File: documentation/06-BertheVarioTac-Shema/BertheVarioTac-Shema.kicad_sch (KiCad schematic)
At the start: 15 parts, among them CN1 4P-1.25 Temperature and humid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, P1 4P-1.25 Power supply base, P1 Potentiometer 10k ohms, P3 4P-1.25 Extended IO, P4 2P-1.25 SPEAK, SW1 SW_DIP_x01

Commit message: son + gps + baro ok
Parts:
- removed R1: R 100 ohms, symbol Device:R_Small
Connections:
- net GNDREF: now also CN1.4 (Pin_4)
- net at P4.1 (Pin_1): now also S1.2
- net at HMC5883L_Mag.. (VIN): now also CN1.1 (Pin_1), GPS-NEO6M. (VCC)
- net at CN1.3 (Pin_3): now also BMP180_Pres.. (VIN), HMC5883L_Mag.. (VIN)
- new net: BMP180_Pres.. (VIN), CN1.2 (Pin_2), HMC5883L_Mag.. (VIN)
- now unconnected: BMP180_Pres.. (VIN), BMP180_Pres.. (VIN), P3.2 (Pin_2)
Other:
- note removed: "NC"
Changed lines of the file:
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@@
-    (stroke (width 0) (type default))
-  )
-  (wire (pts (xy 128.27 52.07) (xy 149.86 52.07))
     (stroke (width 0) (type default))
   )
@@
     (stroke (width 0) (type default))
   )
+  (wire (pts (xy 133.35 59.69) (xy 144.78 59.69))
+    (stroke (width 0) (type default))
+  )
   (wire (pts (xy 170.18 44.45) (xy 170.18 45.72))
     (stroke (width 0) (type default))
@@
     (stroke (width 0) (type default))
   )
-  (wire (pts (xy 53.34 69.85) (xy 57.15 69.85))
-    (stroke (width 0) (type default))
-  )
-  (wire (pts (xy 149.86 73.66) (xy 161.29 73.66))
+  (wire (pts (xy 144.78 73.66) (xy 161.29 73.66))
     (stroke (width 0) (type default))
   )
@@
     (stroke (width 0) (type default))
   )
+  (wire (pts (xy 133.35 76.2) (xy 133.35 59.69))
+    (stroke (width 0) (type default))
+  )
   (wire (pts (xy 220.98 156.21) (xy 220.98 144.78))
     (stroke (width 0) (type default))
   )
-  (wire (pts (xy 149.86 52.07) (xy 149.86 73.66))
-    (stroke (width 0) (type default))
-  )
   (wire (pts (xy 196.85 27.94) (xy 196.85 29.21))
     (stroke (width 0) (type default))
   )
+  (wire (pts (xy 144.78 59.69) (xy 144.78 60.96))
+    (stroke (width 0) (type default))
+  )
   (wire (pts (xy 58.42 130.81) (xy 69.85 130.81))
     (stroke (width 0) (type default))
@@
     (stroke (width 0) (type default))
   )
+  (wire (pts (xy 128.27 76.2) (xy 133.35 76.2))
+    (stroke (width 0) (type default))
+  )
+  (wire (pts (xy 128.27 78.74) (xy 144.78 78.74))
+    (stroke (width 0) (type default))
+  )
   (wire (pts (xy 229.87 148.59) (xy 237.49 148.59))
     (stroke (width 0) (type default))
@@
     (stroke (width 0) (type default))
   )
-  (wire (pts (xy 38.1 69.85) (xy 48.26 69.85))
+  (wire (pts (xy 38.1 69.85) (xy 57.15 69.85))
+    (stroke (width 0) (type default))
+  )
+  (wire (pts (xy 144.78 73.66) (xy 144.78 78.74))
     (stroke (width 0) (type default))
   )
@@
     (stroke (width 0) (type default))
   )
-  (text "IO22 SCL" (at 139.7 55.88 0)
+  (text "IO22 SCL" (at 144.78 72.39 0)
     (effects (font (size 1.27 1.27)) (justify left bottom))
   )
@@
     (effects (font (size 1.27 1.27)) (justify left bottom))
   )
-  (text "IO27 SDA" (at 140.97 80.01 0)
+  (text "IO27 SDA" (at 143.51 83.82 0)
     (effects (font (size 1.27 1.27)) (justify left bottom))
   )
@@
   )
   (text "Rx\n" (at 73.66 110.49 0)
-    (effects (font (size 1.27 1.27)) (justify left bottom))
-  )
-  (text "NC" (at 129.54 78.74 0)
     (effects (font (size 1.27 1.27)) (justify left bottom))
   )
@@
   (text "Tx" (at 72.39 135.89 0)
     (effects (font (size 1.27 1.27)) (justify left bottom))
-  )
-  (symbol (lib_id "Device:R_Small") (at 50.8 69.85 270) (unit 1)
-    (in_bom yes) (on_board yes) (dnp no) (fields_autoplaced)
-    (property "Reference" "R1" (at 50.8 64.77 90)
-      (effects (font (size 1.27 1.27)))
-    )
-    (property "Value" "R 100 ohms" (at 50.8 67.31 90)
-      (effects (font (size 1.27 1.27)))
-    )
-    (property "Footprint" "" (at 50.8 69.85 0)
-      (effects (font (size 1.27 1.27)) hide)
-    )
-    (property "Datasheet" "~" (at 50.8 69.85 0)
-      (effects (font (size 1.27 1.27)) hide)
-    )
-    (pin "1")
-    (pin "2")
-    (instances
-      (project "BertheVarioTac-Shema"
-        (path "/20a72893-107a-4d28-9717-d104a5df1eab"
-          (reference "R1") (unit 1)
-        )
-      )
-    )
   )
   (symbol (lib_id "BertheLibrary:I2C-COMPOSANT") (at 203.2 105.41 0) (unit 1)
@@
         )
       )
+    )
+  )
+  (symbol (lib_id "power:GNDREF") (at 144.78 60.96 0) (unit 1)
+    (in_bom yes) (on_board yes) (dnp no) (fields_autoplaced)
+    (property "Reference" "#PWR06" (at 144.78 67.31 0)
+      (effects (font (size 1.27 1.27)) hide)
+    )
+    (property "Value" "GNDREF" (at 144.78 66.04 0)
+      (effects (font (size 1.27 1.27)))
+    )
+    (property "Footprint" "" (at 144.78 60.96 0)
+      (effects (font (size 1.27 1.27)) hide)
+    )
+    (property "Datasheet" "" (at 144.78 60.96 0)
+      (effects (font (size 1.27 1.27)) hide)
+    )
+    (pin "1")
+    (instances
+      (project "BertheVarioTac-Shema"
+        (path "/20a72893-107a-4d28-9717-d104a5df1eab"
+          (reference "#PWR06") (unit 1)
+        )
+      )

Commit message: anti-rebond bouton
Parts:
- added 1/2w: 18 ohms, symbol Device:R_Small
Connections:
- net at HMC5883L_Mag.. (VIN): now also CN1.1 (Pin_1), GPS-NEO6M. (VCC)
- net at P4.1 (Pin_1): now also 1/2w.2; no longer S1.2
- net VDD: no longer names the net of Lipo-1S-to-5V. (OUT_5V), P1.1 (Pin_1)
- new net: BMP180_Pres.. (VIN), CN1.2 (Pin_2), HMC5883L_Mag.. (VIN)
- new net: BMP180_Pres.. (VIN), CN1.3 (Pin_3), HMC5883L_Mag.. (VIN)
- new net: 1/2w.1, S1.2
- now unconnected: BMP180_Pres.. (VIN), BMP180_Pres.. (VIN)
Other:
- note added: "Vdd to Out Battery converter"
- note removed: "to Vdd Out Battery converter"

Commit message: capteur magnetique ok
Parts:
- renumbered HMC5883L_Mag. to QMC5883_Mag.
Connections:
- net at QMC5883_Mag.. (VIN): now also CN1.1 (Pin_1), GPS-NEO6M. (VCC)
- new net: BMP180_Pres.. (VIN), CN1.2 (Pin_2), QMC5883_Mag.. (VIN)
- new net: BMP180_Pres.. (VIN), CN1.3 (Pin_3), QMC5883_Mag.. (VIN)
- now unconnected: BMP180_Pres.. (VIN), BMP180_Pres.. (VIN)
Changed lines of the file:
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@@
   (symbol (lib_id "BertheLibrary:I2C-COMPOSANT") (at 203.2 105.41 0) (unit 1)
     (in_bom yes) (on_board yes) (dnp no)
-    (property "Reference" "HMC5883L_Mag." (at 196.85 105.41 0)
+    (property "Reference" "QMC5883_Mag." (at 196.85 105.41 0)
       (effects (font (size 1.27 1.27)) (justify left))
     )
@@
       (project "BertheVarioTac-Shema"
         (path "/20a72893-107a-4d28-9717-d104a5df1eab"
-          (reference "HMC5883L_Mag.") (unit 1)
+          (reference "QMC5883_Mag.") (unit 1)
         )
       )

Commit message: modification shema kicad
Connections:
- net at QMC5883_Mag.. (VIN): now also CN1.1 (Pin_1), GPS-NEO6M. (VCC)
- net at 1/2w.2, P4.1 (Pin_1): now also 1/2w.1, S1.2
- new net: BMP180_Pres.. (VIN), CN1.2 (Pin_2), QMC5883_Mag.. (VIN)
- new net: BMP180_Pres.. (VIN), CN1.3 (Pin_3), QMC5883_Mag.. (VIN)
- now unconnected: BMP180_Pres.. (VIN), BMP180_Pres.. (VIN)
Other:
- note added: "ou shunt suivant preference"
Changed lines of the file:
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@@
   (junction (at 196.85 27.94) (diameter 0) (color 0 0 0 0)
   )
+  (junction (at 53.34 69.85) (diameter 0) (color 0 0 0 0)
+  )
   (junction (at 158.75 78.74) (diameter 0) (color 0 0 0 0)
+  )
+  (junction (at 40.64 69.85) (diameter 0) (color 0 0 0 0)
   )
   (junction (at 161.29 73.66) (diameter 0) (color 0 0 0 0)
@@
     (stroke (width 0) (type default))
   )
-  (wire (pts (xy 49.53 69.85) (xy 57.15 69.85))
+  (wire (pts (xy 49.53 69.85) (xy 53.34 69.85))
     (stroke (width 0) (type default))
   )
@@
     (stroke (width 0) (type default))
   )
+  (wire (pts (xy 53.34 54.61) (xy 53.34 69.85))
+    (stroke (width 0) (type default))
+  )
+  (wire (pts (xy 53.34 69.85) (xy 57.15 69.85))
+    (stroke (width 0) (type default))
+  )
   (wire (pts (xy 227.33 34.29) (xy 227.33 27.94))
     (stroke (width 0) (type default))
@@
     (stroke (width 0) (type default))
   )
+  (wire (pts (xy 40.64 69.85) (xy 40.64 54.61))
+    (stroke (width 0) (type default))
+  )
   (wire (pts (xy 158.75 78.74) (xy 189.23 78.74))
     (stroke (width 0) (type default))
@@
     (stroke (width 0) (type default))
   )
-  (wire (pts (xy 38.1 69.85) (xy 44.45 69.85))
+  (wire (pts (xy 38.1 69.85) (xy 40.64 69.85))
     (stroke (width 0) (type default))
   )
@@
     (stroke (width 0) (type default))
   )
+  (wire (pts (xy 40.64 69.85) (xy 44.45 69.85))
+    (stroke (width 0) (type default))
+  )
   (wire (pts (xy 95.25 119.38) (xy 95.25 129.54))
     (stroke (width 0) (type default))
@@
   )
   (wire (pts (xy 128.27 76.2) (xy 133.35 76.2))
+    (stroke (width 0) (type default))
+  )
+  (wire (pts (xy 40.64 54.61) (xy 53.34 54.61))
     (stroke (width 0) (type default))
   )
@@
     (effects (font (size 1.27 1.27)) (justify left bottom))
   )
+  (text "ou shunt suivant preference" (at 34.29 53.34 0)
+    (effects (font (size 1.27 1.27)) (justify left bottom))
+  )

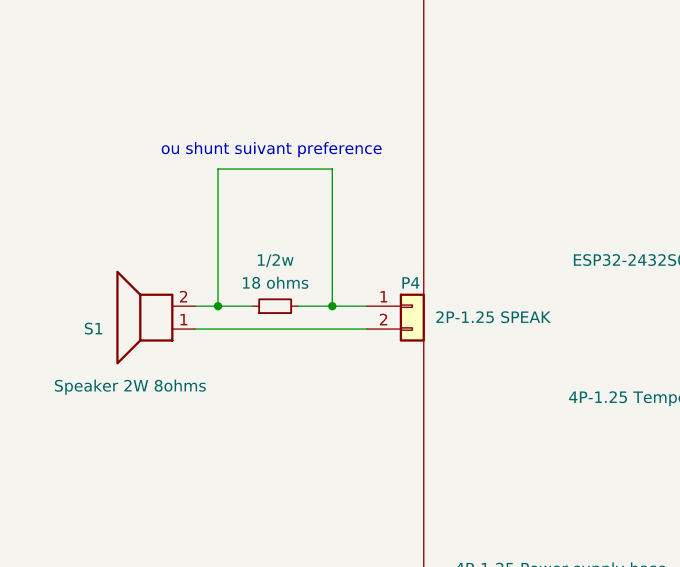
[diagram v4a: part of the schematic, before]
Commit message: modification conditions en vol
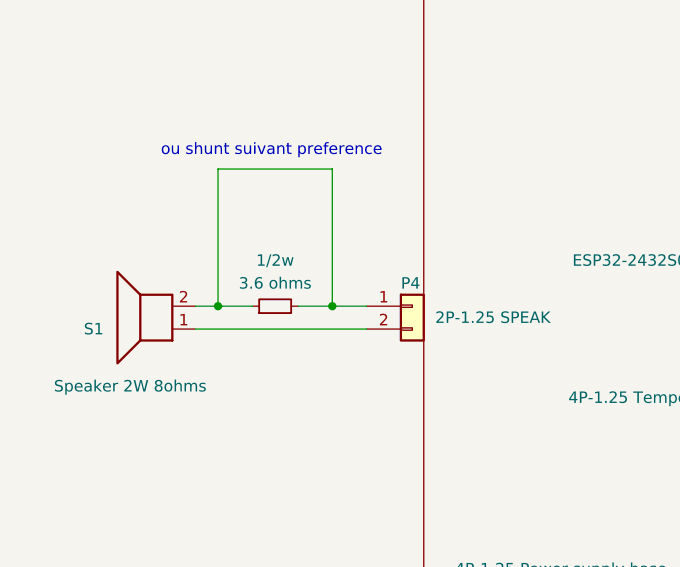
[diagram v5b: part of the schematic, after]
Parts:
- 1/2w: value 18 ohms -> 3.6 ohms
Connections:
- net at QMC5883_Mag.. (VIN): now also CN1.1 (Pin_1), GPS-NEO6M. (VCC)
- new net: BMP180_Pres.. (VIN), CN1.2 (Pin_2), QMC5883_Mag.. (VIN)
- new net: BMP180_Pres.. (VIN), CN1.3 (Pin_3), QMC5883_Mag.. (VIN)
- now unconnected: BMP180_Pres.. (VIN), BMP180_Pres.. (VIN)
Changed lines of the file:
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@@
   (title_block
     (title "BertheVarioTac")
-    (date "2024-10-04")
+    (date "2024-10-05")
     (rev "1.0")
     (comment 1 "Author : SpinBerthe")
@@
       (effects (font (size 1.27 1.27)))
     )
-    (property "Value" "18 ohms" (at 46.99 67.31 90)
-      (effects (font (size 1.27 1.27)))
-    )
+    (property "Value" "3.6 ohms" (at 46.99 67.31 90)
+      (effects (font (size 1.27 1.27)))
+    )

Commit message: essai pcb
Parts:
- removed BMP180_Pres.: ~, symbol BertheLibrary:I2C-COMPOSANT
- added BMP180_Press.1: ~, BertheShema:4 trous standard, symbol BertheLibrary:carre_simple
- BT1, P4, S1, SW1: footprint (none) -> BertheShema:2 trous standard
- CN1, P1, P3: footprint (none) -> BertheShema:4 trous standard
- ESP32-2432S028_WROOM-32: value ~ -> -; footprint (none) -> Symbol:KiCad-Logo2_5mm_SilkScreen
- GPS-NEO6M1: renamed from GPS-NEO6M; value ~ -> -; footprint (none) -> BertheShema:4 trous standard
- Lipo-1S-to-5V1: renamed from Lipo-1S-to-5V; value ~ -> -; footprint (none) -> BertheShema:3 trous standard
- P5: renamed from P1; value Potentiometer 10k ohms -> 10 k ohms; footprint (none) -> Potentiometer_THT:Potentiometer_ACP_CA14-H4_Horizontal
- QMC5883_Mag.1: renamed from QMC5883_Mag.; value ~ -> -; footprint (none) -> BertheShema:4 trous standard
- R1: renamed from 1/2w; footprint (none) -> Resistor_THT:R_Axial_DIN0207_L6.3mm_D2.5mm_P10.16mm_Horizontal
- Usb-C-charger1: renamed from Usb-C-charger; value ~ -> -; footprint (none) -> BertheShema:2 trous standard
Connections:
- net GNDREF: now also CN1.1 (Pin_1), BMP180_Press.1.1 (GND); no longer CN1.4 (Pin_4)
- net at QMC5883_Mag.1. (VIN): now also CN1.4 (Pin_4), GPS-NEO6M1. (VCC), BMP180_Press.1.4 (VCC)
- net at CN1.2 (Pin_2), QMC5883_Mag.1. (VIN): now also BMP180_Press.1.2 (SCL)
- net at CN1.3 (Pin_3), QMC5883_Mag.1. (VIN): now also BMP180_Press.1.3 (SDA)
- net at P4.1 (Pin_1), R1.2: no longer R1.1, S1.2
- new net: R1.1, S1.2
- no-connect marks 5 -> 2
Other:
- note removed: "+3.3V to BMP180"
- note removed: "3.3v"
- moved on the sheet: CN1

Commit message: modification pcb
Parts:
- removed QMC5883_Mag.1: -, BertheShema:4 trous standard, symbol BertheLibrary:I2C-COMPOSANT
- added QMC5883_Mag1: ~, BertheShema:QMC5883, symbol BertheLibrary:QMC5883
- CN1: value 4P-1.25 Temperature and humidity interface -> Temperature and humidity interface
- P1: value 4P-1.25 Power supply base -> Power supply base
- P3: value 4P-1.25 Extended IO -> Extended IO
- P4: value 2P-1.25 SPEAK -> SPEAK
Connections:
- net GNDREF: now also QMC5883_Mag1.3 (GND)
- net at BMP180_Press.1.2 (SCL), CN1.2 (Pin_2): now also QMC5883_Mag1.2 (SCL)
- net at BMP180_Press.1.3 (SDA), CN1.3 (Pin_3): now also QMC5883_Mag1.1 (SDA)
- net at BMP180_Press.1.4 (VCC), CN1.4 (Pin_4), GPS-NEO6M1. (VCC): now also QMC5883_Mag1.4 (VIN)
- no-connect marks 2 -> 1
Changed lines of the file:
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@@
   (junction (at 77.47 110.49) (diameter 0) (color 0 0 0 0)
   )
-  (junction (at 158.75 78.74) (diameter 0) (color 0 0 0 0)
+  (junction (at 185.42 78.74) (diameter 0) (color 0 0 0 0)
+  )
+  (junction (at 176.53 73.66) (diameter 0) (color 0 0 0 0)
   )
   (junction (at 95.25 119.38) (diameter 0) (color 0 0 0 0)
@@
   (junction (at 40.64 69.85) (diameter 0) (color 0 0 0 0)
   )
-  (junction (at 161.29 73.66) (diameter 0) (color 0 0 0 0)
-  )
   (junction (at 196.85 20.32) (diameter 0) (color 0 0 0 0)
   )
@@
   )
   (no_connect (at 99.06 119.38))
-  (no_connect (at 181.61 99.06))
   (wire (pts (xy 170.18 55.88) (xy 181.61 55.88))
     (stroke (width 0) (type default))
@@
     (stroke (width 0) (type default))
   )
+  (wire (pts (xy 185.42 78.74) (xy 189.23 78.74))
+    (stroke (width 0) (type default))
+  )
   (wire (pts (xy 77.47 110.49) (xy 77.47 107.95))
     (stroke (width 0) (type default))
@@
     (stroke (width 0) (type default))
   )
+  (wire (pts (xy 176.53 102.87) (xy 189.23 102.87))
+    (stroke (width 0) (type default))
+  )
   (wire (pts (xy 227.33 34.29) (xy 227.33 27.94))
     (stroke (width 0) (type default))
   )
-  (wire (pts (xy 158.75 78.74) (xy 158.75 107.95))
-    (stroke (width 0) (type default))
-  )
-  (wire (pts (xy 128.27 78.74) (xy 158.75 78.74))
+  (wire (pts (xy 176.53 73.66) (xy 176.53 102.87))
     (stroke (width 0) (type default))
   )
@@
     (stroke (width 0) (type default))
   )
-  (wire (pts (xy 181.61 99.06) (xy 189.23 99.06))
-    (stroke (width 0) (type default))
-  )
   (wire (pts (xy 166.37 20.32) (xy 196.85 20.32))
     (stroke (width 0) (type default))
@@
     (stroke (width 0) (type default))
   )
+  (wire (pts (xy 176.53 73.66) (xy 189.23 73.66))
+    (stroke (width 0) (type default))
+  )
   (wire (pts (xy 40.64 69.85) (xy 40.64 54.61))
     (stroke (width 0) (type default))
@@
     (stroke (width 0) (type default))
   )
-  (wire (pts (xy 158.75 78.74) (xy 189.23 78.74))
+  (wire (pts (xy 128.27 78.74) (xy 185.42 78.74))
     (stroke (width 0) (type default))
   )
@@
     (stroke (width 0) (type default))
   )
-  (wire (pts (xy 144.78 73.66) (xy 161.29 73.66))
+  (wire (pts (xy 144.78 73.66) (xy 176.53 73.66))
     (stroke (width 0) (type default))
   )
@@
     (stroke (width 0) (type default))
   )
+  (wire (pts (xy 185.42 99.06) (xy 189.23 99.06))
+    (stroke (width 0) (type default))
+  )
   (wire (pts (xy 58.42 156.21) (xy 220.98 156.21))
     (stroke (width 0) (type default))
@@
     (stroke (width 0) (type default))
   )
-  (wire (pts (xy 161.29 102.87) (xy 189.23 102.87))
-    (stroke (width 0) (type default))
-  )
   (wire (pts (xy 72.39 133.35) (xy 189.23 133.35))
     (stroke (width 0) (type default))
@@
     (stroke (width 0) (type default))
   )
+  (wire (pts (xy 161.29 107.95) (xy 189.23 107.95))
+    (stroke (width 0) (type default))
+  )
   (wire (pts (xy 236.22 20.32) (xy 196.85 20.32))
     (stroke (width 0) (type default))
   )
-  (wire (pts (xy 161.29 73.66) (xy 161.29 102.87))
-    (stroke (width 0) (type default))
-  )
   (wire (pts (xy 134.62 81.28) (xy 134.62 100.33))
     (stroke (width 0) (type default))
   )
-  (wire (pts (xy 158.75 107.95) (xy 189.23 107.95))
-    (stroke (width 0) (type default))
-  )
   (wire (pts (xy 69.85 130.81) (xy 69.85 107.95))
     (stroke (width 0) (type default))
@@
     (stroke (width 0) (type default))
   )
+  (wire (pts (xy 185.42 78.74) (xy 185.42 99.06))
+    (stroke (width 0) (type default))
+  )
   (wire (pts (xy 229.87 148.59) (xy 237.49 148.59))
     (stroke (width 0) (type default))
   )
   (wire (pts (xy 196.85 44.45) (xy 229.87 44.45))
-    (stroke (width 0) (type default))
-  )
-  (wire (pts (xy 161.29 73.66) (xy 189.23 73.66))
     (stroke (width 0) (type default))
   )
@@
     (effects (font (size 1.27 1.27)) (justify left bottom))
   )
-  (text "GND\n\n" (at 175.26 101.6 0)
-    (effects (font (size 1.27 1.27)) (justify left bottom))
-  )
   (text "ou shunt suivant preference" (at 34.29 53.34 0)
     (effects (font (size 1.27 1.27)) (justify left bottom))
@@
     (effects (font (size 1.27 1.27)) (justify left bottom))
   )
-  (symbol (lib_id "BertheLibrary:I2C-COMPOSANT") (at 203.2 105.41 0) (unit 1)
-    (in_bom yes) (on_board yes) (dnp no)
-    (property "Reference" "QMC5883_Mag.1" (at 196.85 105.41 0)
-      (effects (font (size 1.27 1.27)) (justify left))
-    )
-    (property "Value" "-" (at 203.2 105.41 0)
-      (effects (font (size 1.27 1.27)) hide)
-    )
-    (property "Footprint" "BertheShema:4 trous standard" (at 203.2 105.41 0)
-      (effects (font (size 1.27 1.27)) hide)
-    )
-    (property "Datasheet" "" (at 203.2 105.41 0)
-      (effects (font (size 1.27 1.27)) hide)
-    )
-    (pin "")
-    (pin "")
-    (pin "")
-    (pin "")
-    (instances
-      (project "BertheVarioTac-Shema"
-        (path "/20a72893-107a-4d28-9717-d104a5df1eab"
-          (reference "QMC5883_Mag.1") (unit 1)
+  (symbol (lib_id "BertheLibrary:QMC5883") (at 196.85 105.41 0) (unit 1)
+    (in_bom yes) (on_board yes) (dnp no)
+    (property "Reference" "QMC5883_Mag1" (at 196.85 104.14 0)
+      (effects (font (size 1.27 1.27)) (justify left))
+    )
+    (property "Value" "~" (at 196.85 105.41 0)
+      (effects (font (size 1.27 1.27)))
+    )
+    (property "Footprint" "BertheShema:QMC5883" (at 196.85 105.41 0)
+      (effects (font (size 1.27 1.27)) hide)
+    )
+    (property "Datasheet" "" (at 196.85 105.41 0)
+      (effects (font (size 1.27 1.27)) hide)
+    )
+    (pin "1")
+    (pin "2")
+    (pin "4")
+    (pin "3")
+    (instances
+      (project "BertheVarioTac-Shema"
+        (path "/20a72893-107a-4d28-9717-d104a5df1eab"
+          (reference "QMC5883_Mag1") (unit 1)
         )
       )
@@
       (effects (font (size 1.27 1.27)) (justify left))
     )
-    (property "Value" "2P-1.25 SPEAK" (at 64.77 71.12 0)
+    (property "Value" "SPEAK" (at 64.77 71.12 0)
       (effects (font (size 1.27 1.27)) (justify left))
     )
@@
       (effects (font (size 1.27 1.27)))
     )
-    (property "Value" "4P-1.25 Power supply base" (at 78.74 99.06 90)
+    (property "Value" "Power supply base" (at 74.93 99.06 90)
       (effects (font (size 1.27 1.27)))
     )
@@
       (effects (font (size 1.27 1.27)))
     )
-    (property "Value" "4P-1.25 Temperature and humidity interface" (at 99.06 77.47 0)
+    (property "Value" "Temperature and humidity interface" (at 104.14 77.47 0)
       (effects (font (size 1.27 1.27)))
     )
@@
       (effects (font (size 1.27 1.27)))
     )
-    (property "Value" "4P-1.25 Extended IO" (at 110.49 52.07 0)
+    (property "Value" "Extended IO" (at 115.57 50.8 0)
       (effects (font (size 1.27 1.27)))
     )
@@
         )
       )
+    )
+  )
+  (symbol (lib_id "power:GNDREF") (at 161.29 107.95 270) (mirror x) (unit 1)
+    (in_bom yes) (on_board yes) (dnp no)
+    (property "Reference" "#PWR01" (at 154.94 107.95 0)
+      (effects (font (size 1.27 1.27)) hide)
+    )
+    (property "Value" "GNDREF" (at 156.21 107.95 0)
+      (effects (font (size 1.27 1.27)))
+    )
+    (property "Footprint" "" (at 161.29 107.95 0)
+      (effects (font (size 1.27 1.27)) hide)
+    )
+    (property "Datasheet" "" (at 161.29 107.95 0)
+      (effects (font (size 1.27 1.27)) hide)
+    )
+    (pin "1")
+    (instances
+      (project "BertheVarioTac-Shema"
+        (path "/20a72893-107a-4d28-9717-d104a5df1eab"
+          (reference "#PWR01") (unit 1)
+        )
+      )

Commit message: modification pcb
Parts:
- GPS-NEO6M1: footprint BertheShema:4 trous standard -> BertheShema:GPSNEO6V2
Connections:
- net GNDREF: now also GPS-NEO6M1.1 (GND); no longer GPS-NEO6M1. (VCC)
- net at BMP180_Press.1.4 (VCC), CN1.4 (Pin_4), QMC5883_Mag1.4 (VIN): now also GPS-NEO6M1.4 (VCC); no longer GPS-NEO6M1. (VCC)
- net at P1.2 (Pin_2): now also GPS-NEO6M1.2 (TX); no longer GPS-NEO6M1. (VCC)
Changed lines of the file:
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@@
       (effects (font (size 1.27 1.27)) hide)
     )
-    (property "Footprint" "BertheShema:4 trous standard" (at 203.2 135.89 0)
+    (property "Footprint" "BertheShema:GPSNEO6V2" (at 203.2 135.89 0)
       (effects (font (size 1.27 1.27)) hide)
     )
@@
       (effects (font (size 1.27 1.27)) hide)
     )
-    (pin "")
-    (pin "")
-    (pin "")
-    (pin "")
+    (pin "2")
+    (pin "1")
+    (pin "3")
+    (pin "4")
     (instances
       (project "BertheVarioTac-Shema"
